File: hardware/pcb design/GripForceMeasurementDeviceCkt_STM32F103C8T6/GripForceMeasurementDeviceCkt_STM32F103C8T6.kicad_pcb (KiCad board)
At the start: 2 copper layers, 136 x 70 mm, 65 parts, among them J10 Conn_01x32, J11 Conn_01x32, J12 Conn_01x32, J13 Conn_01x32, J14 Conn_01x32, J15 Conn_01x32, J16 Conn_01x32, J17 Conn_01x32, J18 Conn_01x02, J19 Power_Conn, J2 Boot Conn, J5 SWD, J6 Conn_01x03, J7 Gyro_Sensor_ICM_20948_SparkFu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, J8 Conn_01x32, J9 Conn_01x32, P1 USB_C_Plug_USB2.0, SW1 SW_Push, U1 ESP32-C3-Mini, U10 ADG732BSUZ, U11 ADG732BSUZ, U12 ADG732BSUZ, U13 ADG732BSUZ, U14 ADG732BSUZ, U2 FT232RL, U3 LM358, U4 STM32F103C8Tx, U5 ADG732BSUZ, U6 ADG732BSUZ, U7 ADG732BSUZ, U8 ADG732BSUZ, U9 ADG732BSUZ, Y1 8MHz

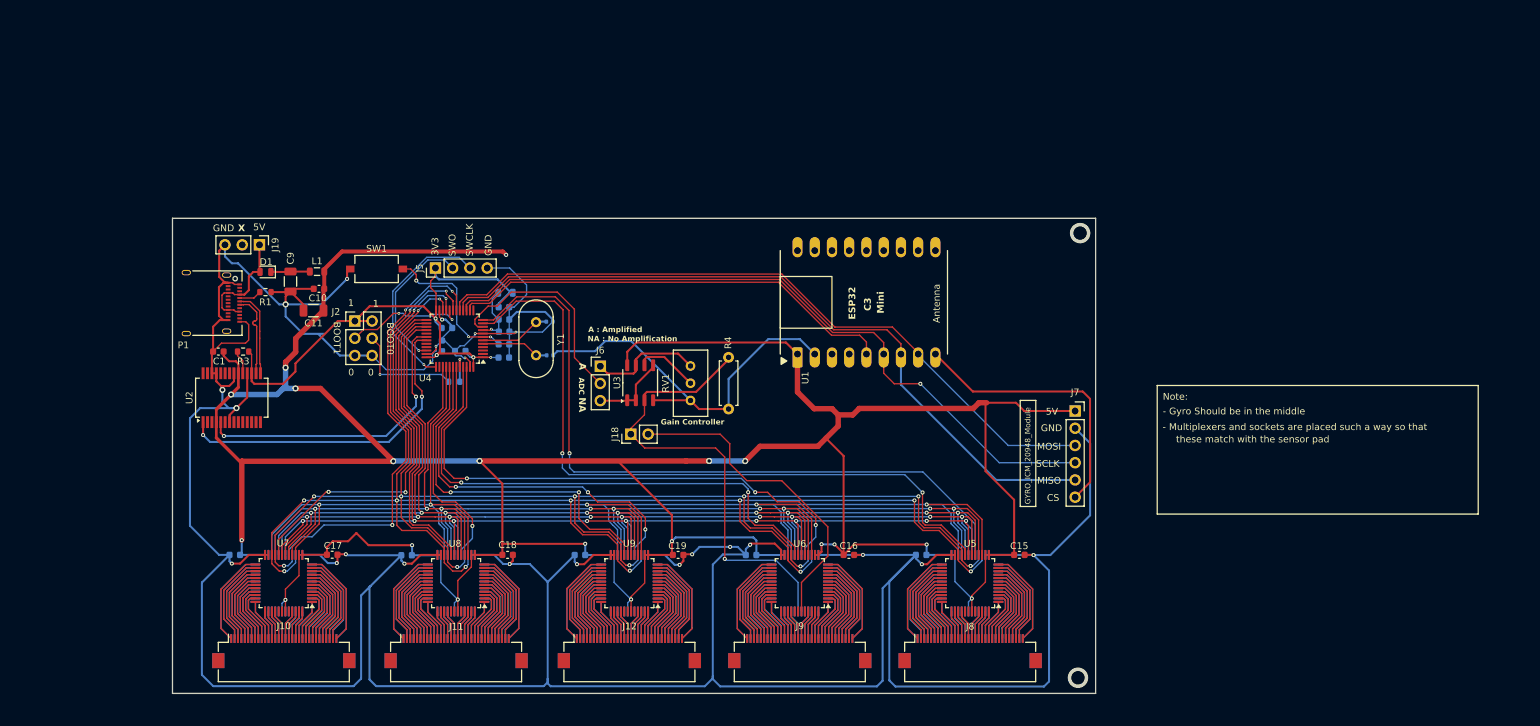
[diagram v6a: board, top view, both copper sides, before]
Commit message: GND ground layer filled
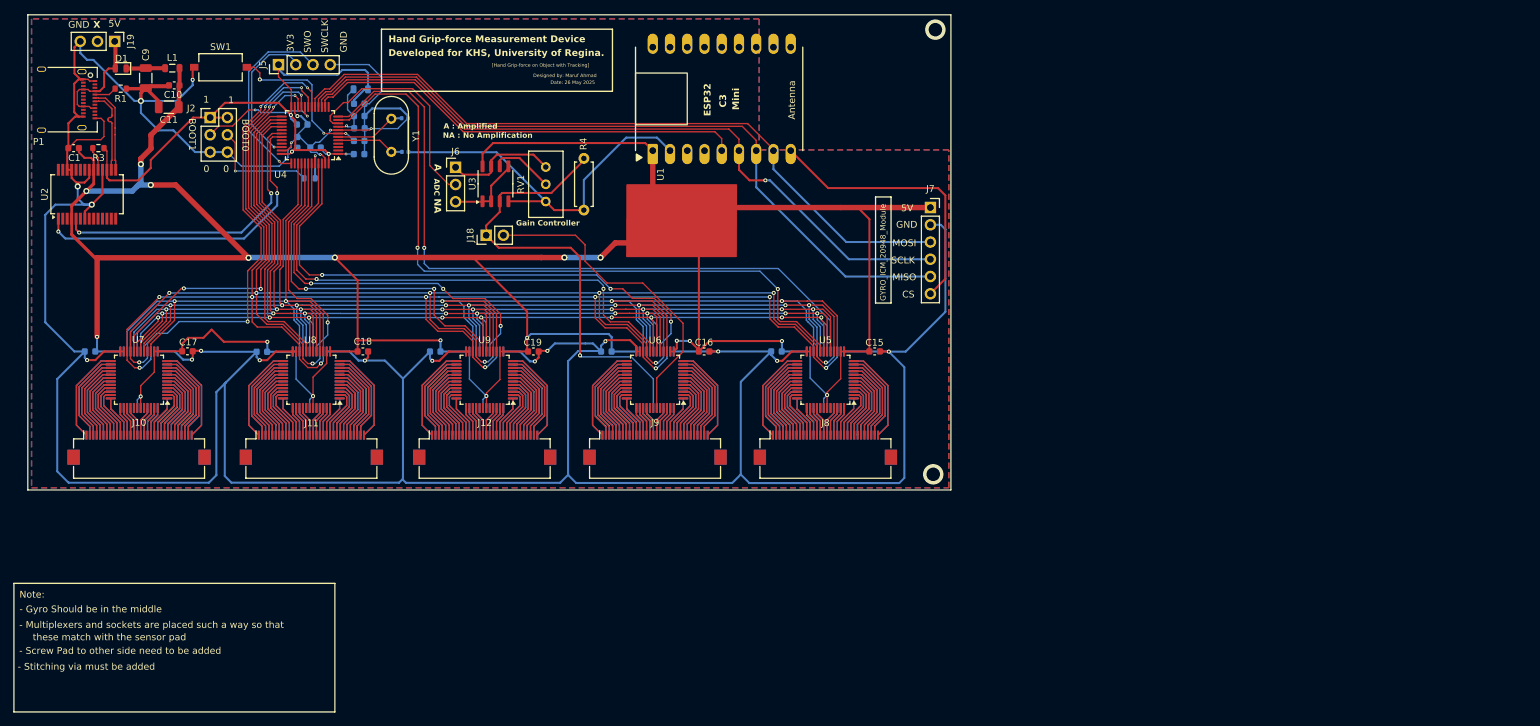
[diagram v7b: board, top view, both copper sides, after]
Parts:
- moved J5 37.8 mm to (69.9, 30.6)
- moved SW1 37.6 mm to (61.4, 31.0)
- moved C12 36.8 mm to (81.8, 41.9)
- moved C21 36.8 mm to (67.5, 72.9)
- moved C22 36.8 mm to (93.0, 72.9)
- moved C24 36.8 mm to (118.2, 72.9)
- moved C6 36.8 mm to (81.8, 38.2)
- moved C8 36.8 mm to (81.8, 36.4)
- moved U10 36.8 mm to (150.5, 77.0)
- moved U11 36.8 mm to (74.8, 77.0)
- moved U12 36.8 mm to (100.3, 77.0)
- moved U4 36.8 mm to (74.6, 41.0)
- moved U5 36.8 mm to (150.5, 77.0)
- moved C10 36.8 mm to (54.6, 33.7)
- moved C9 36.8 mm to (50.4, 32.6)
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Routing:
- net +5V: track 527.5 -> 495.8 mm, vias 19 -> 18
- net GND: track 695.5 -> 675.6 mm, vias 22 -> 21
- net +3.3V: track 89.0 -> 91.8 mm
- net /NRST: track 22.4 -> 24.0 mm
- net ADC: track 31.9 -> 33.2 mm
- net MOSI: track 104.3 -> 105.5 mm
- net SENSOR_OUT_L: track 47.9 -> 47.3 mm
- net SENSOR_OUT_R: track 68.3 -> 67.7 mm
- added copper zone on B.Cu, net GND
- added copper zone on F.Cu, net GND
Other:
- board text added: "- Screw Pad to other side need to be added"
- board text added: "- Stitching via must be added"
- board text added: "Date: 26 May 2025"
- board text added: "Designed by: Maruf Ahmad"
- board text added: "Developed for KHS, University of Regina."
- board text added: "Hand Grip-force Measurement Device"
- board text added: "[Hand Grip-force on Object with Tracking]"

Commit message: Firmware develepment initiated
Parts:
- added D2: LED-Red, LED_SMD:LED_0603_1608Metric, F.Cu at (79.3, 48.7)
- added D3: LED-Green, LED_SMD:LED_0603_1608Metric, F.Cu at (82.2, 48.7)
- added R3: 510R, Resistor_SMD:R_0603_1608Metric, F.Cu at (79.3, 52.9)
- added R4: 510R, Resistor_SMD:R_0603_1608Metric, F.Cu at (82.2, 52.9)
- C13, C14: footprint Capacitor_SMD:C_0402_1005Metric -> Capacitor_SMD:C_0603_1608Metric
- D1: footprint Diode_SMD:D_MicroMELF -> Diode_SMD:D_SOD-323_HandSoldering
- L1: footprint Inductor_SMD:L_0805_2012Metric -> Inductor_SMD:L_0603_1608Metric
- R6: renamed from R4; footprint Resistor_THT:R_Axial_DIN0207_L6.3mm_D2.5mm_P7.62mm_Horizontal -> Resistor_THT:R_Axial_DIN0207_L6.3mm_D2.5mm_P10.16mm_Horizontal
- moved C14 0.57 mm to (89.1, 38.5)
- moved C13 0.53 mm to (89.1, 43.5)
- renumbered C2 to C1, C3 to C2, C4 to C3, C5 to C4, C6 to C5, C7 to C6, C8 to C7, C1 to C8, J19 to J1, J8 to J10, J9 to J11, J10 to J12, J11 to J13, J12 to J14, J13 to J15, J14 to J16, J15 to J17, J16 to J18, J17 to J19, J2 to J3, J18 to J6, J6 to J7, J7 to J9, R3 to R5
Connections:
- U4 pad 2: unconnected-(U4-PC13-Pad2) -> PC13
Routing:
- net PC13: track 0.00 -> 14.2 mm
- net +3.3V: track 91.8 -> 98.3 mm
- net GND: track 675.6 -> 680.1 mm, vias 21 -> 40
- net Net-(D3-K): track 0.00 -> 2.59 mm
- net Net-(D2-K): track 0.00 -> 2.58 mm
- net SENSOR_OUT_L: track 47.3 -> 46.5 mm
- net (no net): vias 2 -> 0
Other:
- outline, holes or cut-outs redrawn
- board text added: "ADG732BSUZ"
- board text added: "Designed by: Maruf Ahmad, SaskTechLab"
- board text added: "Developed for URNeuroLab, University of Regina"
- board text added: "FT232RL"
- board text added: "LM358"
- board text added: "ON"
- board text added: "PC13"
- board text added: "Reference: www.urneurolab.com www.sasktechlab.com"
- board text added: "STM32F103C8T6"
- board text added: "Sparkfun 9DoF IMU Breakout ICM-20948"
- board text added: "WaveShare-ESP32-C3-Mini-Dev-Board"
- board text removed: "Designed by: Maruf Ahmad"
- board text removed: "Developed for KHS, University of Regina."
